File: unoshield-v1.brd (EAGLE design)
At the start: 54.6 x 63.5 mm, 24 parts, among them Q1 FDS5680, X1 SPRING-TERMINAL, X2 SPRING-TERMINAL

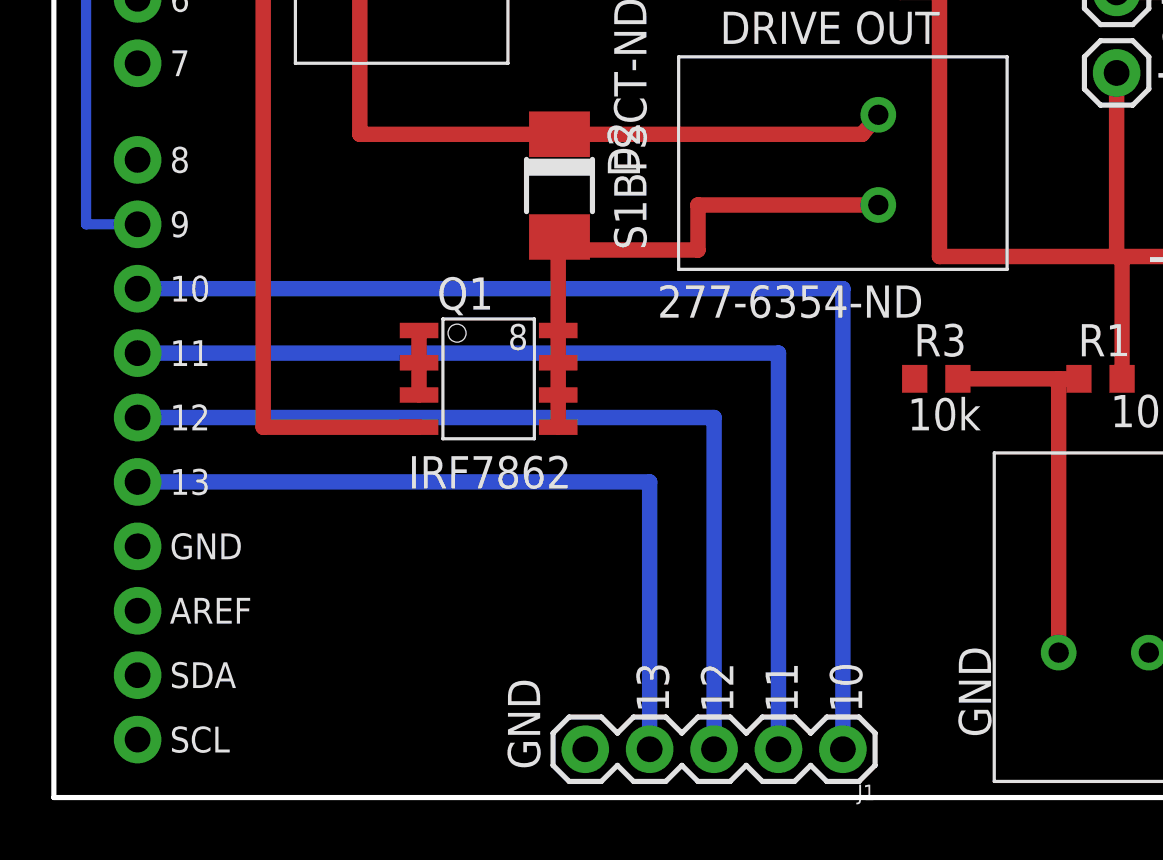
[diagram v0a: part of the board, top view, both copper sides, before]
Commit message: added external digital I/O line
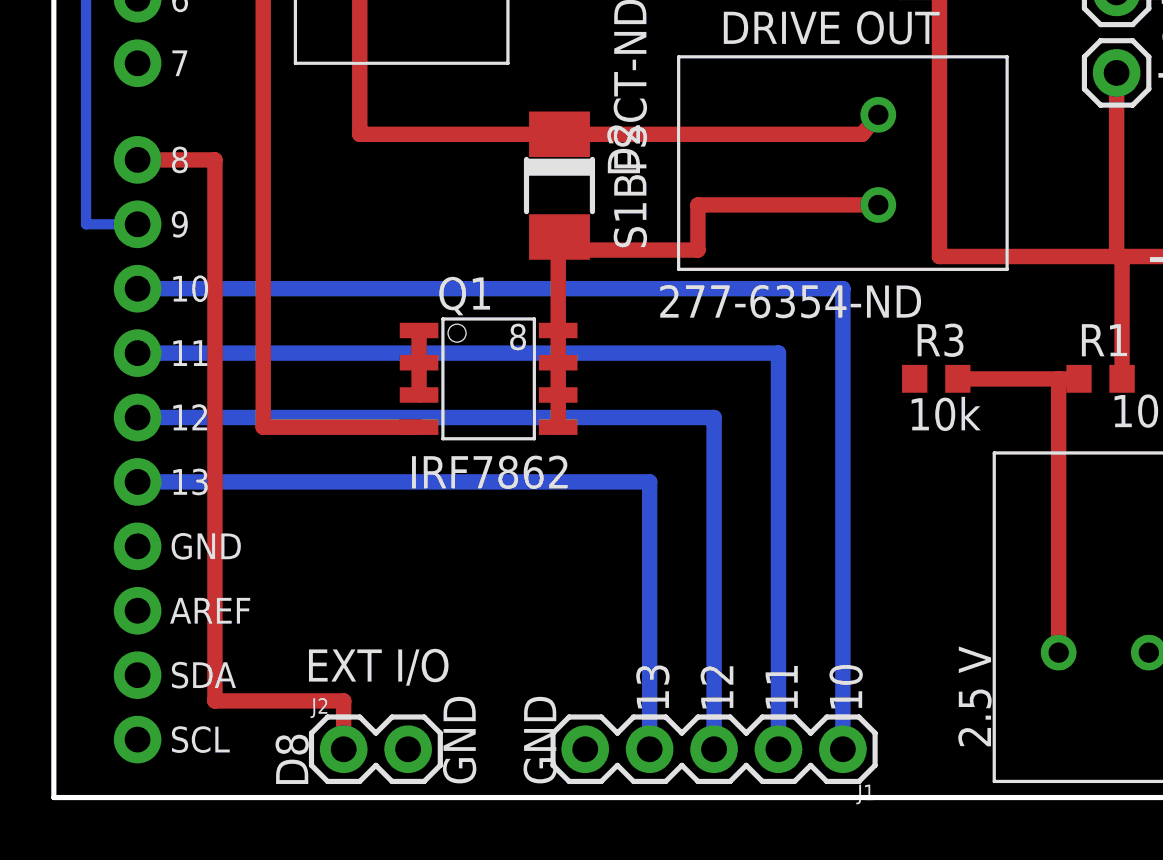
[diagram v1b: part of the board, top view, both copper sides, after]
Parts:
- added J2: (no value), SparkFun-Connectors:1X02
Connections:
- new net N$13: J2.1, U$1.D8
- net GND: now also J2.2
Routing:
- net N$13: track 0.00 -> 31.4 mm
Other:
- board text added: "2.5 V"
- board text added: "D8"
- board text added: "EXT I/O"
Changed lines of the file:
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@@
 <text x="47.625" y="60.706" size="1.778" layer="21">I2C</text>
 <text x="43.561" y="22.225" size="1.778" layer="21" rot="R180">+</text>
-<text x="34.417" y="5.969" size="1.27" layer="21" rot="R270">GND</text>
+<text x="34.417" y="5.969" size="1.27" layer="21" rot="R270">2.5 V</text>
 <text x="40.386" y="14.605" size="1.27" layer="21">10k</text>
 <text x="32.385" y="14.478" size="1.27" layer="21">10k</text>
@@
 (A0)</text>
 <text x="20.701" y="55.245" size="1.27" layer="21" rot="R180">D3</text>
-<text x="16.637" y="4.699" size="1.27" layer="21" rot="R270">GND</text>
+<text x="17.272" y="4.064" size="1.27" layer="21" rot="R270">GND</text>
 <text x="16.637" y="39.624" size="1.27" layer="21" rot="R270">GND</text>
 <text x="33.655" y="30.988" size="1.27" layer="21" rot="R180">DRIVE OUT</text>
@@
 <text x="26.797" y="5.334" size="1.27" layer="21" rot="R270">11</text>
 <text x="29.337" y="5.334" size="1.27" layer="21" rot="R270">10</text>
+<text x="14.097" y="4.064" size="1.27" layer="21" rot="R270">GND</text>
+<text x="8.763" y="0.381" size="1.27" layer="21" rot="R90">D8</text>
+<text x="8.636" y="4.572" size="1.27" layer="21">EXT I/O</text>
 </plain>
 <attributes>
@@
 <element name="JP11" library="SparkFun-Connectors" package="1X01" value="M01PTH" x="26.67" y="62.23"/>
 <element name="JP12" library="SparkFun-Connectors" package="1X01" value="M01PTH" x="29.21" y="62.23"/>
+<element name="J2" library="SparkFun-Connectors" package="1X02" value="" x="10.16" y="1.905"/>
 </elements>
 <signals>
@@
 <wire x1="13.1318" y1="17.145" x2="13.1318" y2="18.415" width="0.6096" layer="1"/>
 <contactref element="JP12" pad="1"/>
+<contactref element="J2" pad="2"/>
 </signal>
 <signal name="N$1">
@@
 <wire x1="19.05" y1="62.23" x2="19.05" y2="59.69" width="0.6096" layer="1"/>
 </signal>
+<signal name="N$13">
+<contactref element="U$1" pad="D8"/>
+<contactref element="J2" pad="1"/>
+<wire x1="2.032" y1="25.146" x2="5.08" y2="25.146" width="0.6096" layer="1"/>
+<wire x1="5.08" y1="25.146" x2="5.08" y2="3.81" width="0.6096" layer="1"/>
+<wire x1="5.08" y1="3.81" x2="10.16" y2="3.81" width="0.6096" layer="1"/>
+<wire x1="10.16" y1="3.81" x2="10.16" y2="1.905" width="0.6096" layer="1"/>
+</signal>
 </signals>

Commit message: uno shield design work
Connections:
- net GND: now also J1.1; no longer J1.5
- net N$10: now also J1.4; no longer J1.3
- net N$11: now also J1.5; no longer J1.4
- net N$7: now also J1.2; no longer J1.1
- net N$9: now also J1.3; no longer J1.2
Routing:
- net N$11: track 30.7 -> 28.2 mm
- net N$9: track 40.9 -> 38.4 mm
- net N$7: track 46.0 -> 43.4 mm
- net N$10: track 35.8 -> 33.3 mm
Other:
- board text added: "SSW-105-02-G-S SAM1209-05-ND"
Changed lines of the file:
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@@
 (A0)</text>
 <text x="20.701" y="55.245" size="1.27" layer="21" rot="R180">D3</text>
-<text x="17.272" y="4.064" size="1.27" layer="21" rot="R270">GND</text>
+<text x="29.337" y="7.874" size="1.27" layer="21" rot="R270">GND</text>
 <text x="16.637" y="39.624" size="1.27" layer="21" rot="R270">GND</text>
 <text x="33.655" y="30.988" size="1.27" layer="21" rot="R180">DRIVE OUT</text>
 <text x="32.766" y="60.325" size="0.8128" layer="21" rot="R180">   SWITCH
 360-2884-ND</text>
-<text x="21.717" y="5.334" size="1.27" layer="21" rot="R270">13</text>
-<text x="24.257" y="5.334" size="1.27" layer="21" rot="R270">12</text>
-<text x="26.797" y="5.334" size="1.27" layer="21" rot="R270">11</text>
-<text x="29.337" y="5.334" size="1.27" layer="21" rot="R270">10</text>
+<text x="19.177" y="5.334" size="1.27" layer="21" rot="R270">13</text>
+<text x="21.717" y="5.334" size="1.27" layer="21" rot="R270">12</text>
+<text x="24.257" y="5.334" size="1.27" layer="21" rot="R270">11</text>
+<text x="26.797" y="5.334" size="1.27" layer="21" rot="R270">10</text>
 <text x="14.097" y="4.064" size="1.27" layer="21" rot="R270">GND</text>
 <text x="8.763" y="0.381" size="1.27" layer="21" rot="R90">D8</text>
 <text x="8.636" y="4.572" size="1.27" layer="21">EXT I/O</text>
+<text x="17.526" y="8.382" size="1.27" layer="21">SSW-105-02-G-S
+SAM1209-05-ND </text>
+<text x="39.497" y="12.065" size="1.27" layer="21" rot="R270">277-6354-ND</text>
+<text x="12.192" y="40.64" size="1.27" layer="21" rot="R270">277-6354-ND</text>
 </plain>
 <attributes>
@@
 <contactref element="JP6" pad="1"/>
 <contactref element="JP3" pad="1"/>
-<contactref element="J1" pad="5"/>
 <contactref element="JP8" pad="1"/>
 <wire x1="13.1318" y1="15.875" x2="13.1318" y2="17.145" width="0.6096" layer="1"/>
@@
 <contactref element="JP12" pad="1"/>
 <contactref element="J2" pad="2"/>
+<contactref element="J1" pad="1"/>
 </signal>
 <signal name="N$1">
@@
 <wire x1="50.292" y1="36.83" x2="50.292" y2="36.576" width="0.6096" layer="1"/>
 </signal>
-<signal name="N$7">
-<contactref element="U$1" pad="D10"/>
-<contactref element="J1" pad="1"/>
-<wire x1="2.032" y1="20.066" x2="29.845" y2="20.066" width="0.6096" layer="16"/>
-<wire x1="29.845" y1="20.066" x2="29.845" y2="1.905" width="0.6096" layer="16"/>
-</signal>
-<signal name="N$9">
-<contactref element="J1" pad="2"/>
-<contactref element="U$1" pad="D11"/>
-<wire x1="2.032" y1="17.526" x2="27.305" y2="17.526" width="0.6096" layer="16"/>
-<wire x1="27.305" y1="17.526" x2="27.305" y2="1.905" width="0.6096" layer="16"/>
-</signal>
-<signal name="N$10">
-<contactref element="U$1" pad="D12"/>
-<contactref element="J1" pad="3"/>
-<wire x1="2.032" y1="14.986" x2="18.415" y2="14.986" width="0.6096" layer="16"/>
-<wire x1="18.415" y1="14.986" x2="24.765" y2="14.986" width="0.6096" layer="16"/>
-<wire x1="24.765" y1="14.986" x2="24.765" y2="1.905" width="0.6096" layer="16"/>
-</signal>
-<signal name="N$11">
-<contactref element="U$1" pad="D13"/>
-<contactref element="J1" pad="4"/>
-<wire x1="2.032" y1="12.446" x2="22.225" y2="12.446" width="0.6096" layer="16"/>
-<wire x1="22.225" y1="12.446" x2="22.225" y2="1.905" width="0.6096" layer="16"/>
-</signal>
 <signal name="N$12">
 <contactref element="JP9" pad="1"/>
@@
 <wire x1="10.16" y1="3.81" x2="10.16" y2="1.905" width="0.6096" layer="1"/>
 </signal>
+<signal name="N$7">
+<contactref element="U$1" pad="D10"/>
+<contactref element="J1" pad="2"/>
+<wire x1="2.032" y1="20.066" x2="27.305" y2="20.066" width="0.6096" layer="16"/>
+<wire x1="27.305" y1="20.066" x2="27.305" y2="1.905" width="0.6096" layer="16"/>
+</signal>
+<signal name="N$9">
+<contactref element="J1" pad="3"/>
+<contactref element="U$1" pad="D11"/>
+<wire x1="2.032" y1="17.526" x2="24.765" y2="17.526" width="0.6096" layer="16"/>
+<wire x1="24.765" y1="17.526" x2="24.765" y2="1.905" width="0.6096" layer="16"/>
+</signal>
+<signal name="N$10">
+<contactref element="U$1" pad="D12"/>
+<contactref element="J1" pad="4"/>
+<wire x1="2.032" y1="14.986" x2="22.225" y2="14.986" width="0.6096" layer="16"/>
+<wire x1="22.225" y1="14.986" x2="22.225" y2="1.905" width="0.6096" layer="16"/>
+</signal>
+<signal name="N$11">
+<contactref element="J1" pad="5"/>
+<contactref element="U$1" pad="D13"/>
+<wire x1="2.032" y1="12.446" x2="19.685" y2="12.446" width="0.6096" layer="16"/>
+<wire x1="19.685" y1="12.446" x2="19.685" y2="1.905" width="0.6096" layer="16"/>
+</signal>
 </signals>
